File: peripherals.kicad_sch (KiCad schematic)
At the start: 13 parts, among them J2 GPS_ANT, U5 BME280, U6 LSM303AGR, U7 MAX-M10S

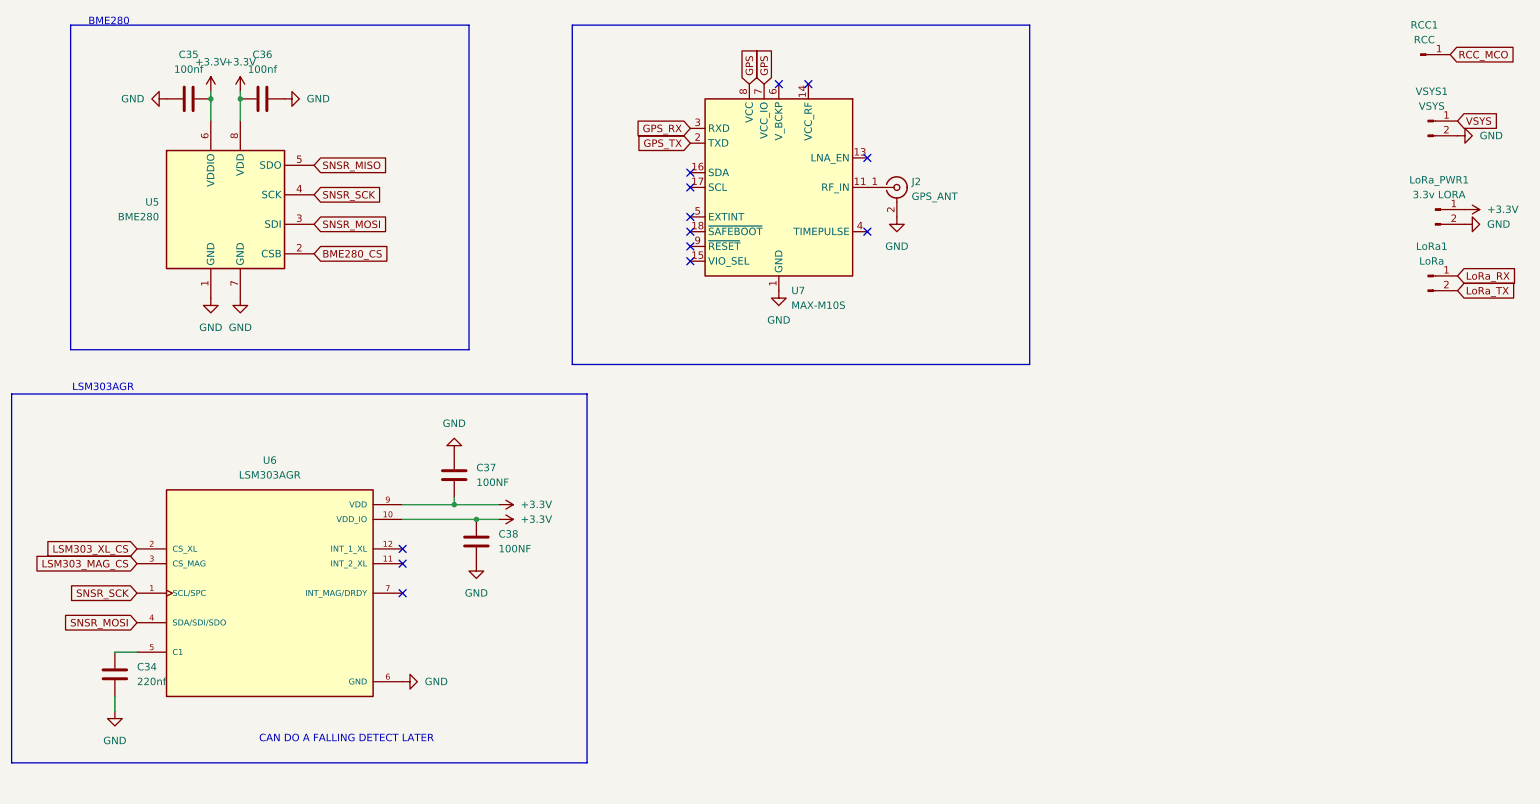
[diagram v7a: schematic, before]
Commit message: Updated with new power rails, added sensors and gps symbol
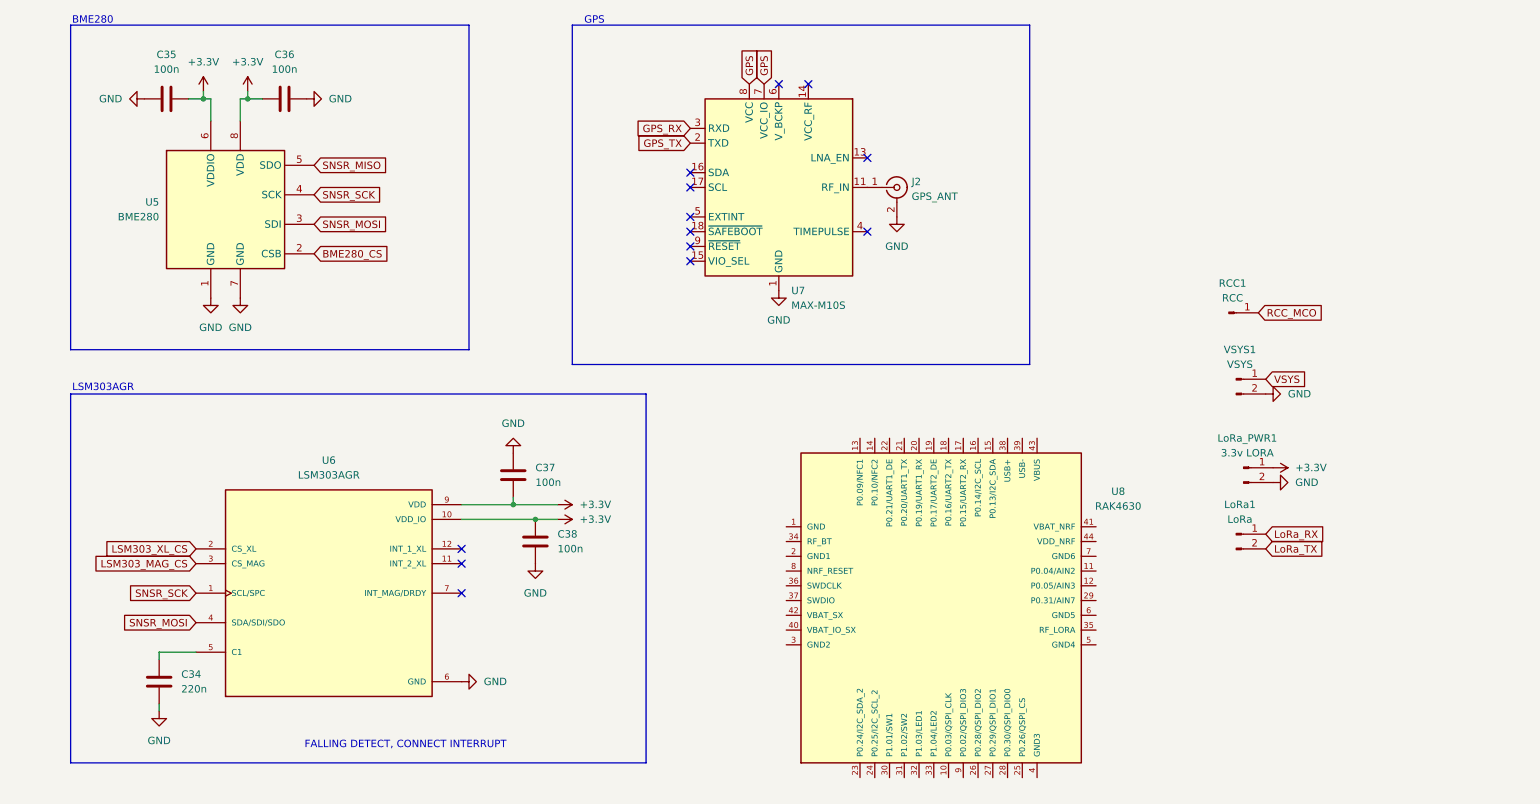
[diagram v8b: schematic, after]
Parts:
- added U8: RAK4630, RAK4630:RAK4630, symbol TheSummitProject:RAK4630
- C34: value 220nf -> 220n
- C35, C36: value 100nf -> 100n
- C37, C38: value 100NF -> 100n
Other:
- note added: "FALLING DETECT, CONNECT INTERRUPT"
- note added: "GPS"
- note removed: "CAN DO A FALLING DETECT LATER"
- moved on the sheet: C34, C35, C36, C37, C38, LoRa1, LoRa_PWR1, RCC1, U6, VSYS1
